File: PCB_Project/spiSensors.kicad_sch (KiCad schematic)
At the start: 0 parts

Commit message: added barebones SPI sensors
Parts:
- added C1, C2, C3: 10nF, symbol Device:C
- added C4, C5, C6, C7: 100nF, symbol Device:C
- added U1: ~, symbol Sensor_Motion:ICM-40609-D
- added U2: ~, symbol Sensor_Motion:BMI088
- added U3: ~, symbol Sensor_Motion:ISM330DHCXTR_
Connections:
- new net 3.3V: C1.2, C2.2, C3.2, C6.1, C7.1, U1.13 (VDD), U1.8 (VDDIO), U3.5 (VDDIO), U3.8 (VDD)
- new net CS: U3.12 (CS)
- new net CSB_Accel_BMI088: U2.14 (CSB1)
- new net CSB_Gryo_BMI088: U2.5 (CSB2)
- new net GND: C1.1, C2.1, C3.1, C4.2, C5.2, C6.2, C7.2, U1.11 (RESV), U1.18 (GND), U1.20 (RESV), U2.2 (NC), U2.4 (GND), U2.6 (GNDIO), U2.7 (PS), U3.6 (GND), U3.7 (GND)
- new net INT1_Accel_BMI: U2.16 (INT1)
- new net INT1_ICM: U1.12 (INT1_/_INT)
- new net INT1_ISM: U3.4 (INT1)
- new net INT2 / FSYNC_ICM: U1.19 (INT2_/_FSYNC)
- new net INT2_Accel_BMI: U2.1 (INT2)
- new net INT2_ISM: U3.9 (INT2)
- new net INT3_Gyro_BMI: U2.12 (INT3)
- new net INT4_Gyro_BMI: U2.13 (INT4)
- new net MISO: U2.10 (SDO2), U2.15 (SDO1)
- new net MOSI: U2.9 (SDI)
- new net MSCL: U3.3 (MSCL)
- new net MSDA: U3.2 (MSDA)
- new net SCK: U2.8 (SCK)
- new net SCL: U3.13 (SCL)
- new net SCLK: U1.23 (SCLK)
- new net SDA: U3.14 (SDA)
- new net SDI: U1.24 (SDI)
- new net SDO: U1.9 (SDO), U3.1 (SDO)
- new net VDD: C5.1, U2.3 (VDD)
- new net VDDIO: C4.1, U2.11 (VDDIO)
- new net nCS: U1.22 (nCS)
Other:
- note added: "BMI088 Accelerometer and Gyroscope"
- note added: "ICM-40609-D Accelerometer and Gyroscope"
- note added: "ISM330DHCXTR Accelerometer and Gyroscope"

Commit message: cleanup
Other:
- moved on the sheet: C1, C2, C3, C4, C5, C6, C7, U1, U2, U3

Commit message: added power board
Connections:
- net VDD is gone; now on net 3V3: C5.1, U2.3 (VDD)
- net VDDIO is gone; now on net 3V3: C4.1, U2.11 (VDDIO)
- net 3.3V renamed 3V3
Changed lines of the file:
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@@
     )
   )
-  (global_label "3.3V" (shape input) (at 38.735 115.57 180) (fields_autoplaced)
+  (global_label "3V3" (shape input) (at 38.735 115.57 180) (fields_autoplaced)
     (effects (font (size 1.27 1.27)) (justify right))
-    (property "Intersheetrefs" "${INTERSHEET_REFS}" (at 31.7168 115.57 0)
+    (property "Intersheetrefs" "${INTERSHEET_REFS}" (at 32.3216 115.57 0)
       (effects (font (size 1.27 1.27)) (justify right) hide)
     )
@@
     )
   )
-  (global_label "3.3V" (shape input) (at 261.62 94.615 0) (fields_autoplaced)
+  (global_label "3V3" (shape input) (at 261.62 94.615 0) (fields_autoplaced)
     (effects (font (size 1.27 1.27)) (justify left))
-    (property "Intersheetrefs" "${INTERSHEET_REFS}" (at 268.6382 94.615 0)
+    (property "Intersheetrefs" "${INTERSHEET_REFS}" (at 268.0334 94.615 0)
       (effects (font (size 1.27 1.27)) (justify left) hide)
     )
@@
     )
   )
-  (global_label "3.3V" (shape input) (at 229.87 106.68 180) (fields_autoplaced)
+  (global_label "3V3" (shape input) (at 229.87 106.68 180) (fields_autoplaced)
     (effects (font (size 1.27 1.27)) (justify right))
-    (property "Intersheetrefs" "${INTERSHEET_REFS}" (at 222.8518 106.68 0)
+    (property "Intersheetrefs" "${INTERSHEET_REFS}" (at 223.4566 106.68 0)
       (effects (font (size 1.27 1.27)) (justify right) hide)
     )
@@
     )
   )
-  (global_label "VDD" (shape input) (at 193.675 92.71 0) (fields_autoplaced)
+  (global_label "3V3" (shape input) (at 193.675 92.71 0) (fields_autoplaced)
     (effects (font (size 1.27 1.27)) (justify left))
-    (property "Intersheetrefs" "${INTERSHEET_REFS}" (at 200.2094 92.71 0)
+    (property "Intersheetrefs" "${INTERSHEET_REFS}" (at 200.0884 92.71 0)
       (effects (font (size 1.27 1.27)) (justify left) hide)
     )
@@
     )
   )
-  (global_label "3.3V" (shape input) (at 90.805 97.155 0) (fields_autoplaced)
+  (global_label "3V3" (shape input) (at 90.805 97.155 0) (fields_autoplaced)
     (effects (font (size 1.27 1.27)) (justify left))
-    (property "Intersheetrefs" "${INTERSHEET_REFS}" (at 97.8232 97.155 0)
+    (property "Intersheetrefs" "${INTERSHEET_REFS}" (at 97.2184 97.155 0)
       (effects (font (size 1.27 1.27)) (justify left) hide)
     )
@@
     )
   )
-  (global_label "VDDIO" (shape input) (at 173.355 96.52 0) (fields_autoplaced)
+  (global_label "3V3" (shape input) (at 173.355 96.52 0) (fields_autoplaced)
     (effects (font (size 1.27 1.27)) (justify left))
-    (property "Intersheetrefs" "${INTERSHEET_REFS}" (at 181.8247 96.52 0)
+    (property "Intersheetrefs" "${INTERSHEET_REFS}" (at 179.7684 96.52 0)
       (effects (font (size 1.27 1.27)) (justify left) hide)
     )

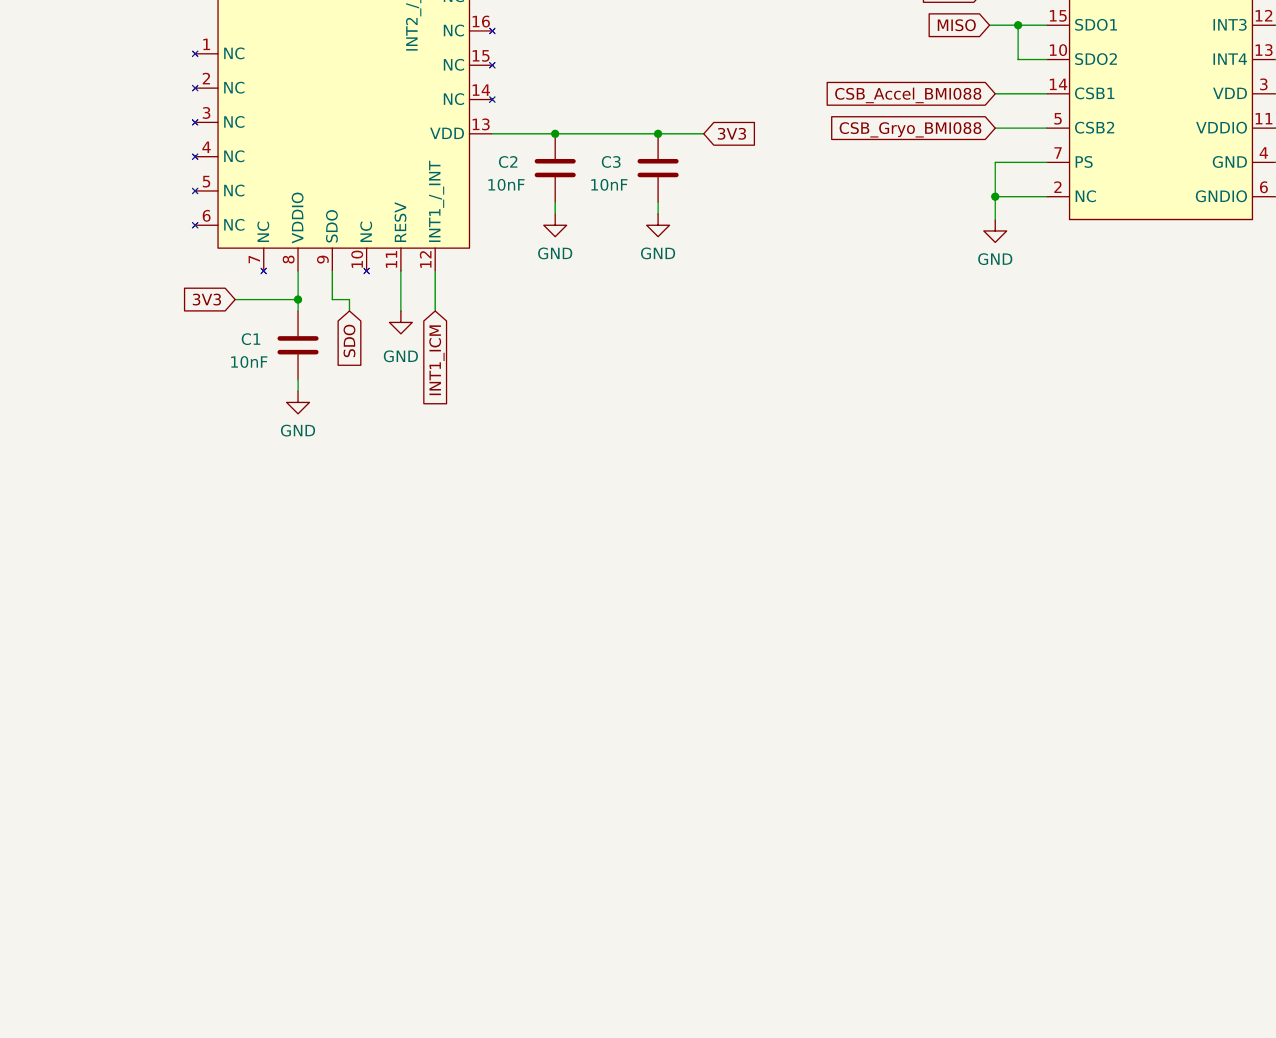
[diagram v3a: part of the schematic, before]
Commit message: ADC mostly added
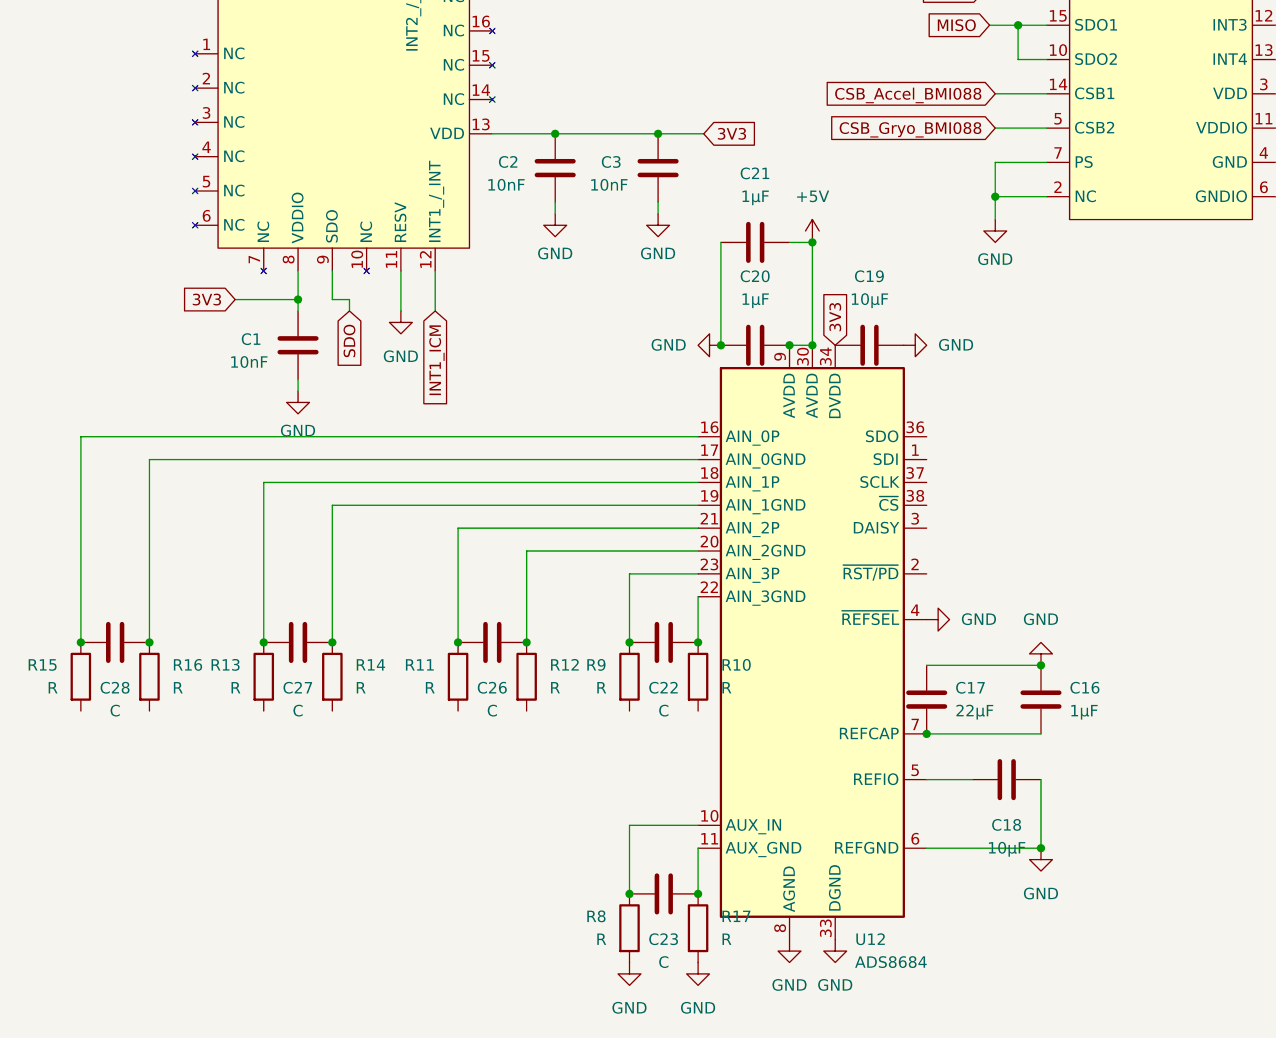
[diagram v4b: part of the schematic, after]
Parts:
- added C16, C20, C21: 1µF, symbol Device:C
- added C17: 22µF, symbol Device:C
- added C18, C19: 10µF, symbol Device:C
- added C22, C23, C26, C27, C28: C, symbol Device:C
- added R10, R11, R12, R13, R14, R15, R16, R17, R8, R9: R, symbol Device:R
- added U12: ADS8684, Package_SO:TSSOP-38_4.4x9.7mm_P0.5mm, symbol Analog_ADC:ADS8684
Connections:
- net 3V3: now also C19.1, U12.34 (DVDD)
- net GND: now also C16.1, C17.1, C18.1, C19.2, C20.1, C21.1, R17.2, R8.2, U12.28 (AGND), U12.29 (AGND), U12.31 (AGND), U12.32 (AGND), U12.33 (DGND), U12.4 (~{REFSEL}), U12.6 (REFGND), U12.8 (AGND)
- new net: C18.2, U12.5 (REFIO)
- new net: C16.2, C17.2, U12.7 (REFCAP)
- new net: C23.2, R8.1, U12.10 (AUX_IN)
- new net: C23.1, R17.1, U12.11 (AUX_GND)
- new net: C28.2, R15.1, U12.16 (AIN_0P)
- new net: C28.1, R16.1, U12.17 (AIN_0GND)
- new net: C27.2, R13.1, U12.18 (AIN_1P)
- new net: C27.1, R14.1, U12.19 (AIN_1GND)
- new net: C26.1, R12.1, U12.20 (AIN_2GND)
- new net: C26.2, R11.1, U12.21 (AIN_2P)
- new net: C22.1, R10.1, U12.22 (AIN_3GND)
- new net: C22.2, R9.1, U12.23 (AIN_3P)
- new net +5V: C20.2, C21.2, U12.30 (AVDD), U12.9 (AVDD)

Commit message: begone ADC you are not needed
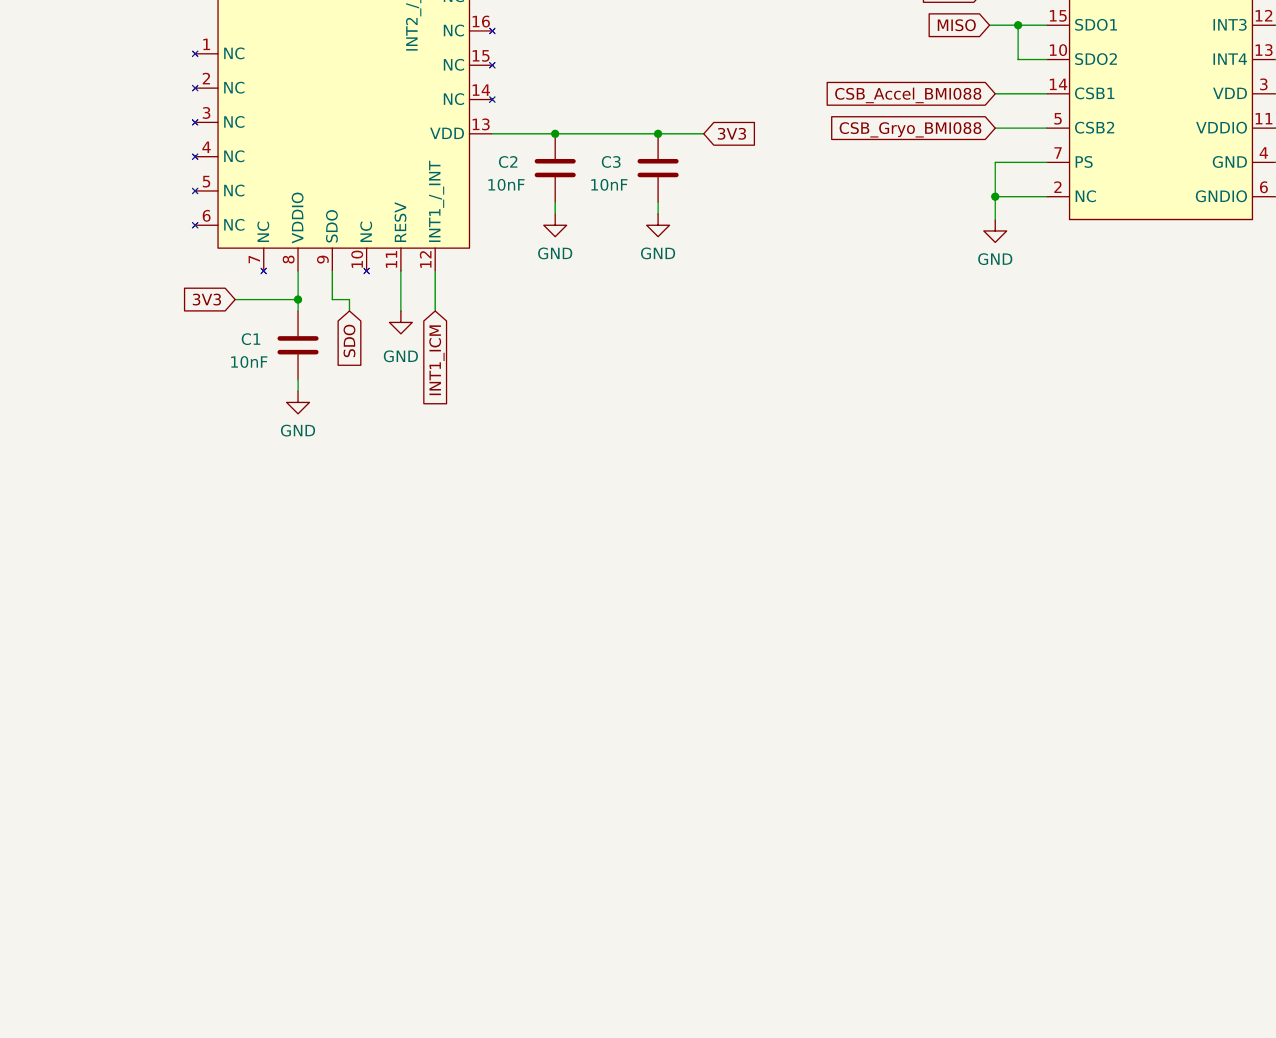
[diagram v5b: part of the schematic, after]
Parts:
- removed C16, C20, C21: 1µF, symbol Device:C
- removed C17: 22µF, symbol Device:C
- removed C18, C19: 10µF, symbol Device:C
- removed C22, C23, C26, C27, C28: C, symbol Device:C
- removed R10, R11, R12, R13, R14, R15, R16, R17, R8, R9: R, symbol Device:R
- removed U12: ADS8684, Package_SO:TSSOP-38_4.4x9.7mm_P0.5mm, symbol Analog_ADC:ADS8684

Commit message: work baby
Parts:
- C1, C4, C5, C6, C7: footprint (none) -> Capacitor_SMD:C_0603_1608Metric
- C2: value 10nF -> 0.1uF; footprint (none) -> Capacitor_SMD:C_0402_1005Metric
- C3: value 10nF -> 2.2uF; footprint (none) -> Capacitor_SMD:C_0402_1005Metric
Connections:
- net MSCL is gone; now on net GND: U3.3 (MSCL)
- net MSDA is gone; now on net GND: U3.2 (MSDA)
- net 3V3 renamed +3V3
- net CS renamed CS_3
- net INT1_Accel_BMI: no longer names the net of U2.16 (INT1)
- net INT1_ICM: no longer names the net of U1.12 (INT1_/_INT)
- net INT1_ISM: no longer names the net of U3.4 (INT1)
- net INT2 / FSYNC_ICM: no longer names the net of U1.19 (INT2_/_FSYNC)
- net INT2_Accel_BMI: no longer names the net of U2.1 (INT2)
- net INT2_ISM: no longer names the net of U3.9 (INT2)
- net INT3_Gyro_BMI: no longer names the net of U2.12 (INT3)
- net INT4_Gyro_BMI: no longer names the net of U2.13 (INT4)
- net MISO renamed SDO_1
- net MOSI renamed SDI_1
- net SCK renamed SCK_1
- net SCL renamed SCL_3
- net SCLK renamed SCLK_2
- net SDA renamed SDA_3
- net SDI renamed SDI_2
- net SDO renamed SDO_2
- net SDO_2: no longer U3.1 (SDO)
- net nCS renamed nCS_2
- new net SDO_3: U3.1 (SDO)
- no-connect marks 0 -> 8
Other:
- moved on the sheet: C1, C2, C3, C4, C5, C7, U1, U2, U3

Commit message: 2 footprints left then can design
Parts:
- C1, C4, C5, C6, C7: footprint Capacitor_SMD:C_0603_1608Metric -> Capacitor_SMD:C_0402_1005Metric
- U2: footprint (none) -> Sensor:QFN_BMI085_BOS
- U3: footprint (none) -> Package_LGA:LGA-14_3x2.5mm_P0.5mm_LayoutBorder3x4y
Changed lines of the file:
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@@
 			)
 		)
-		(property "Footprint" "Capacitor_SMD:C_0603_1608Metric"
+		(property "Footprint" "Capacitor_SMD:C_0402_1005Metric"
 			(at 77.1652 110.49 0)
 			(effects
@@
 			)
 		)
-		(property "Footprint" ""
+		(property "Footprint" "Sensor:QFN_BMI085_BOS"
 			(at 52.07 78.74 0)
 			(effects
@@
 			)
 		)
-		(property "Footprint" "Capacitor_SMD:C_0603_1608Metric"
+		(property "Footprint" "Capacitor_SMD:C_0402_1005Metric"
 			(at 234.6452 114.935 0)
 			(effects
@@
 			)
 		)
-		(property "Footprint" "Capacitor_SMD:C_0603_1608Metric"
+		(property "Footprint" "Capacitor_SMD:C_0402_1005Metric"
 			(at 128.5748 130.81 0)
 			(effects
@@
 			)
 		)
-		(property "Footprint" "Capacitor_SMD:C_0603_1608Metric"
+		(property "Footprint" "Capacitor_SMD:C_0402_1005Metric"
 			(at 75.2348 91.44 0)
 			(effects
@@
 			)
 		)
-		(property "Footprint" ""
+		(property "Footprint" "Package_LGA:LGA-14_3x2.5mm_P0.5mm_LayoutBorder3x4y"
 			(at 236.22 86.36 0)
 			(effects
@@
 			)
 		)
-		(property "Footprint" "Capacitor_SMD:C_0603_1608Metric"
+		(property "Footprint" "Capacitor_SMD:C_0402_1005Metric"
 			(at 254.9652 105.41 0)
 			(effects
